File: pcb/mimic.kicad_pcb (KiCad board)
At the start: 6 copper layers, 50.8 x 22.9 mm, 167 parts, among them J1 Conn_01x12_Male, J2 Conn_01x16_Male, J3 USB_B_Micro, J4 MicroSd, J5 JST, J6 JTAG, SW1 SW_Push, U1 FAN53541, U10 NCP115-2.5, U2 FAN53541, U3 LFE5U-25F-8MG285C, U4 MT41K64M16TW-107_J-TR, U5 BQ24232, U6 W25Q128JVP, U7 FAN53541, U8 TPS51206, U9 74HC4067BQ

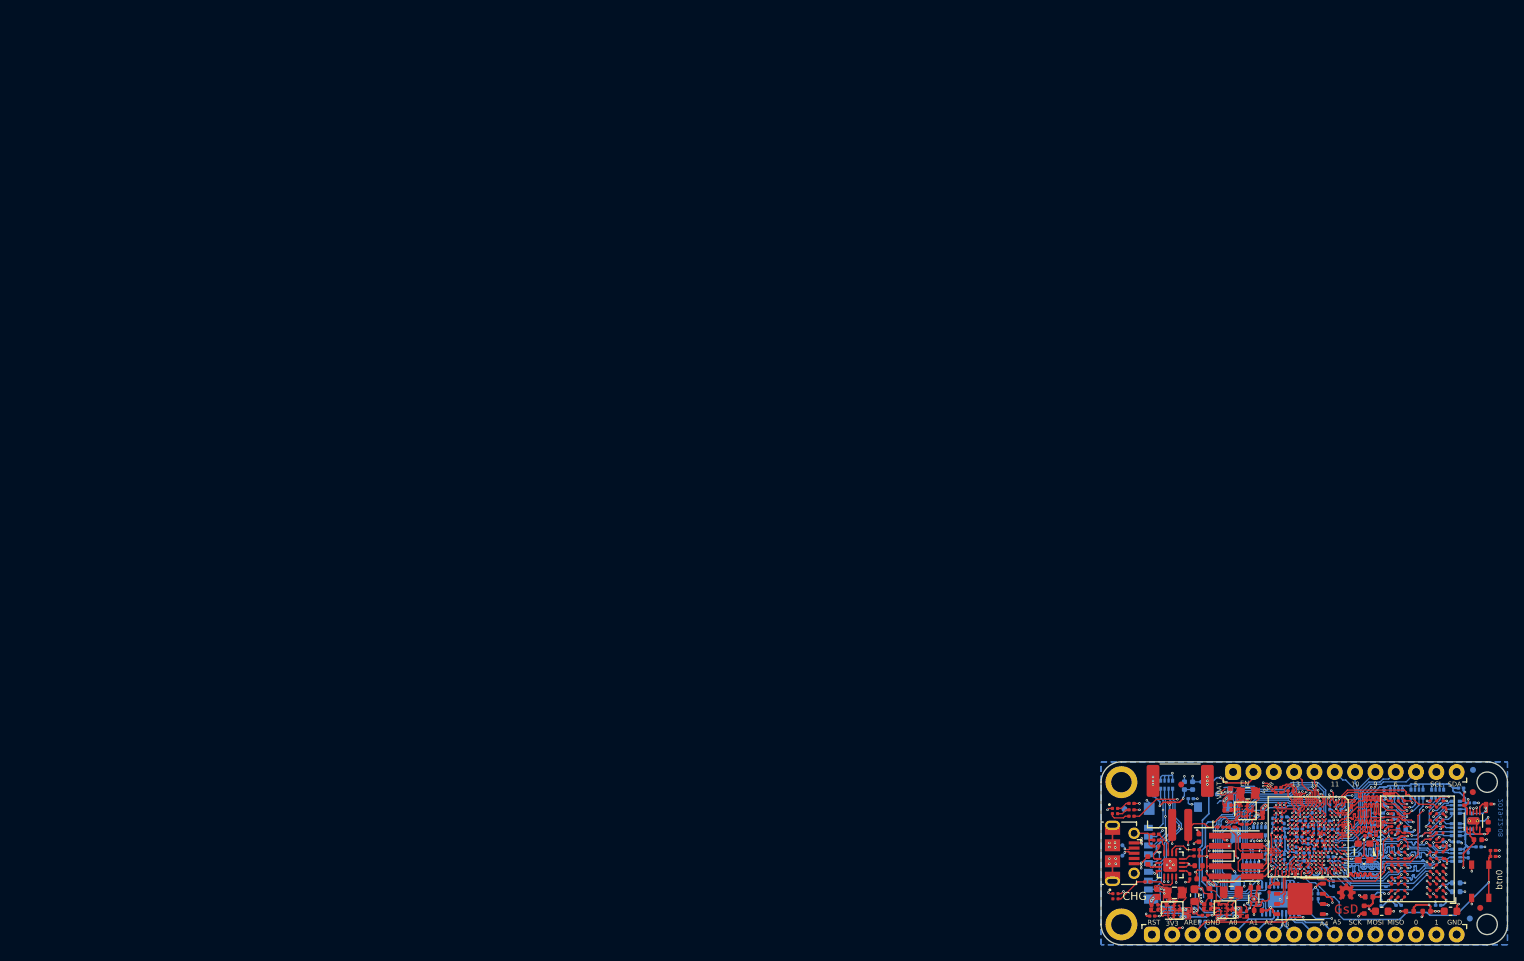
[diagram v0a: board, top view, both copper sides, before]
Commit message: refactor(pcb): strip down
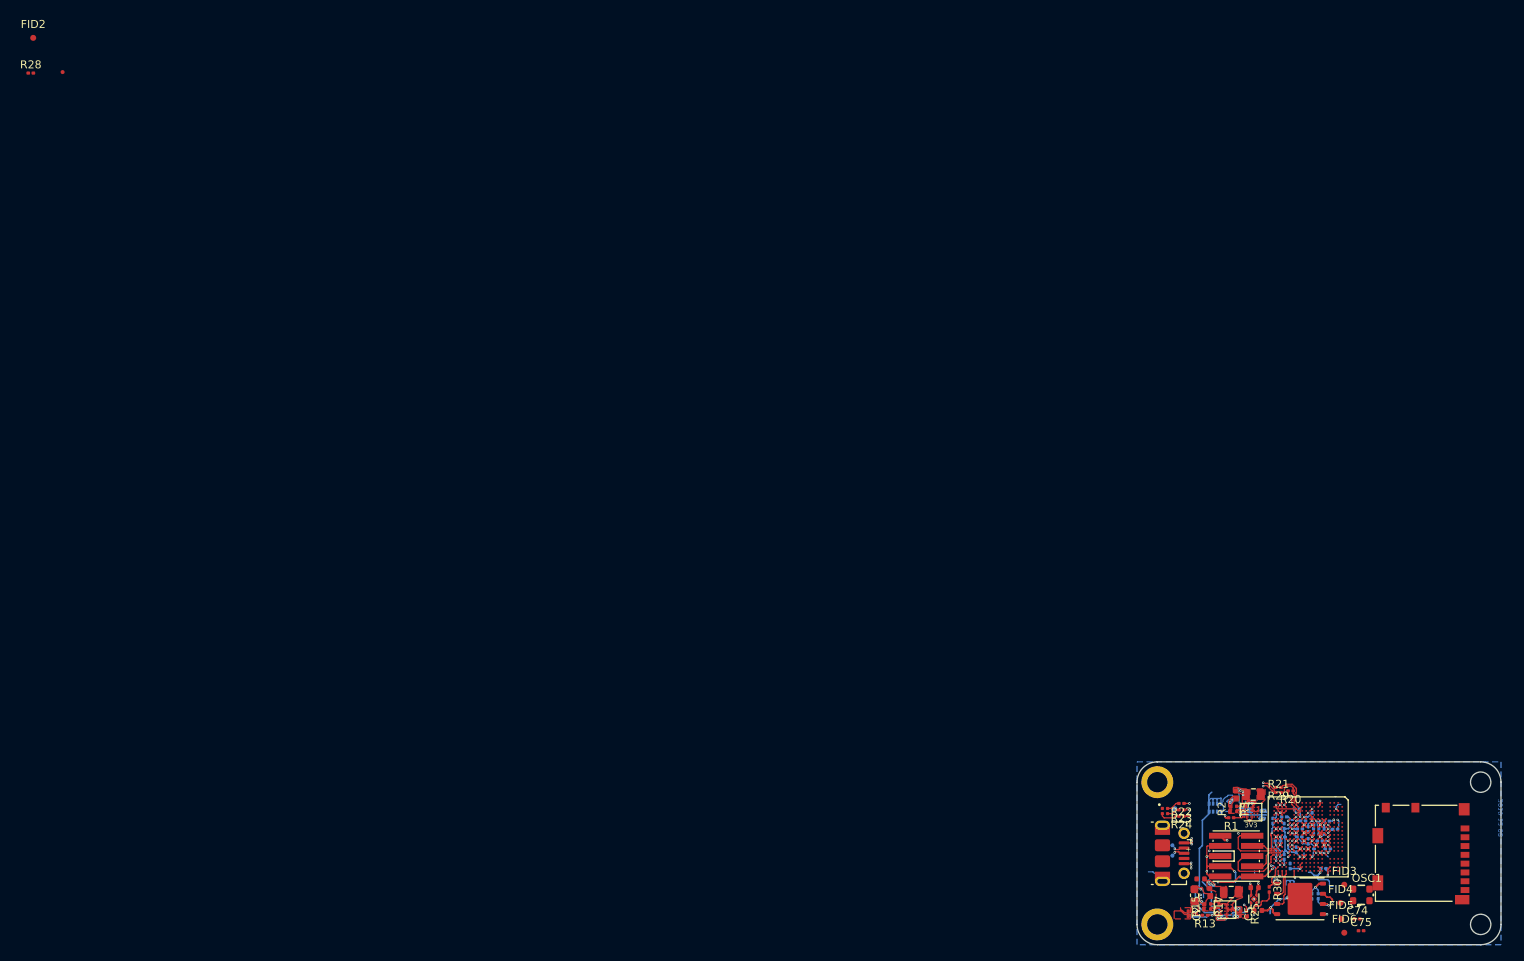
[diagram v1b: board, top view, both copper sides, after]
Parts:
- removed C1, C14, C19, C25, C27, C38, C40, C42, C44, C45, C76: 10nF, gkl_misc:C_0201_0603Metric
- removed C10: 0.22uF, gkl_misc:C_0201_0603Metric
- removed C11, C16, C18, C29, C8: 10uF, Capacitor_SMD:C_0402_1005Metric
- removed C12, C13, C77: 4.7uF, Capacitor_SMD:C_0402_1005Metric
- removed C20, C26, C28, C30, C31, C32, C33, C39, C4, C41, C43, C70, C71, C9: 100nF, gkl_misc:C_0201_0603Metric
- removed C21, C22, C34, C35, C36, C37: 1uF, Capacitor_SMD:C_0402_1005Metric
- removed C23, C24: 22uF, Capacitor_SMD:C_0603_1608Metric
- removed D2: LED_ARGB, gkl_led:0404LED_RGB
- removed FB1, FB2, FB3: 600R, Inductor_SMD:L_0402_1005Metric
- removed G***: LOGO, gkl_logos:oshw_small
- removed G***: LOGO, LOGO
- removed G***: LOGO, logo
- removed J1: Conn_01x12_Male, gkl_conn:Feather_PinHeader_1x12
- removed J2: Conn_01x16_Male, gkl_conn:Feather_PinHeader_1x16
- removed J5: JST, gkl_conn:JST_PH_B2B-PH-SM4-TB_1x02-1MP_P2.00mm_Vertical
- removed L3: 0.47uH, Inductor_SMD:L_0805_2012Metric
- removed R10: 56.2k, gkl_misc:R_0201_0603Metric
- removed R11: 3.06k, gkl_misc:R_0201_0603Metric
- removed R12: 4.32k, gkl_misc:R_0201_0603Metric
- removed R14, R18: 100k, gkl_misc:R_0201_0603Metric
- removed R16: 147k, gkl_misc:R_0201_0603Metric
- removed R19: 240R, Resistor_SMD:R_0402_1005Metric
- removed R26, R32, R33, R7: 10k, gkl_misc:R_0201_0603Metric
- removed R3, R6: 50R, gkl_misc:R_0201_0603Metric
- removed R4, R8: 4.7k, gkl_misc:R_0201_0603Metric
- removed R9: 3.57k, gkl_misc:R_0201_0603Metric
- removed RN1, RN10, RN2, RN3, RN4, RN5, RN6, RN8: 50R, Resistor_SMD:R_Array_Convex_4x0402
- removed RN9: 10K, Resistor_SMD:R_Array_Convex_4x0402
- removed SW1: SW_Push, gkl_misc:PTS_810_SMT_Switch
- removed TP19, TP20, TP28, TP31, TP33: SMD_TP, gkl_misc:TestPoint_Pad_D0.5mm
- removed U4: MT41K64M16TW-107_J-TR, Package_BGA:BGA-96_9.0x13.0mm_Layout2x3x16_P0.8mm
- removed U5: BQ24232, Package_DFN_QFN:QFN-16-1EP_3x3mm_P0.5mm_EP1.75x1.75mm
- removed U7: FAN53541, Package_CSP:WLCSP-20_1.934x2.434mm_Layout4x5_P0.4mm
- removed U8: TPS51206, gkl_housings_dfn:WSON-10-1EP_2x2mm_P0.4mm
- removed U9: 74HC4067BQ, Package_DFN_QFN:Texas_RGY_R-PVQFN-N24_EP2.05x3.1mm
- C2, C48, C49, C5, C50, C51, C52, C53, C54, C55, C56, C57, C58, C59, C60, C61, C62, C63, C64, C65, C66, C67, C68, C69, C74, C75: footprint gkl_misc:C_0201_0603Metric -> Capacitor_SMD:C_0201_0603Metric
- FID3, FID5, J4, TP29: moved to F.Cu
- R1, R13, R15, R17, R2, R20, R21, R22, R23, R24, R25, R27, R29, R30, R31, R5: footprint gkl_misc:R_0201_0603Metric -> Resistor_SMD:R_0201_0603Metric
- R28: footprint gkl_misc:R_0201_0603Metric -> Resistor_SMD:R_0201_0603Metric; moved to F.Cu
- U3: footprint bosonFrameGrabber:csBGA_132 -> gkl_housings_bga:csBGA285
- moved FID2 171.2 mm to (1.02, 1.02)
- moved R28 171.0 mm to (0.72, 5.42), turned to 0 degrees
- moved TP29 167.7 mm to (4.70, 5.30)
- moved J4 39.6 mm to (180.0, 103.0)
- moved FID6 23.8 mm to (164.9, 112.9)
- moved FID3 21.6 mm to (164.9, 106.9)
- moved FID4 17.5 mm to (164.4, 109.2)
- moved FID5 16.1 mm to (164.5, 111.2)
- moved C6 15.8 mm to (151.4, 95.6)
- moved C7 15.8 mm to (152.6, 97.5)
- moved L2 15.8 mm to (153.6, 95.6)
- moved R1 15.8 mm to (150.8, 98.5)
- moved R5 15.8 mm to (151.5, 97.4)
- moved R2 15.8 mm to (150.7, 97.4)
- moved U2 15.8 mm to (153.3, 97.8)
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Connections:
- C62 pad 1: P1.35V -> P3.3V
- C64 pad 1: P1.35V -> P3.3V
- C66 pad 1: P1.35V -> P3.3V
- C68 pad 1: P1.35V -> P3.3V
- J3 pad 4: Net-(J3-Pad4) -> unconnected-(J3-ID-Pad4)
- J4 pad 4: Net-(C29-Pad2) -> unconnected-(J4-Pin_4-Pad4)
- U3 pad A10: SPI_0 -> unconnected-(U3A-PT27B/PCLKC0_1-PadA10)
- U3 pad A11: SPI_2 -> unconnected-(U3A-PT27A/PCLKT0_1-PadA11)
- U3 pad A12: RAM_CS# -> unconnected-(U3F-PL5A-PadA12)
- U3 pad A13: RAM_D7 -> unconnected-(U3F-PL14B-PadA13)
- U3 pad A15: RAM_D4 -> unconnected-(U3F-PL14D-PadA15)
- U3 pad A16: RAM_UDQS- -> unconnected-(U3F-PL20B-PadA16)
- U3 pad A17: RAM_D6 -> unconnected-(U3F-PL23A/PCLKT7_1-PadA17)
- U3 pad A2: RAM_A14 -> unconnected-(U3C-PR20C/GR_PCLK2_0-PadA2)
- U3 pad A3: RAM_A3 -> unconnected-(U3C-PR20A/GR_PCLK2_1-PadA3)
- U3 pad A4: RAM_A4 -> unconnected-(U3C-PR11B-PadA4)
- U3 pad A6: RAM_BA2 -> unconnected-(U3C-PR11A-PadA6)
- U3 pad A7: RAM_A10 -> unconnected-(U3C-PR8B-PadA7)
- U3 pad A8: IO_11 -> unconnected-(U3B-PT35B/PCLKC1_0-PadA8)
- U3 pad B1: RAM_A8 -> unconnected-(U3C-PR23B/PCLKC2_1-PadB1)
- U3 pad B10: IO_5 -> unconnected-(U3A-PT29A/PCLKT0_0-PadB10)
- U3 pad B11: SPI_3 -> unconnected-(U3A-PT4A-PadB11)
- U3 pad B12: RAM_WE# -> unconnected-(U3F-PL2B-PadB12)
- U3 pad B13: RAM_D5 -> unconnected-(U3F-PL14A-PadB13)
- U3 pad B15: RAM_UDQS+ -> unconnected-(U3F-PL20A/GR_PCLK7_1-PadB15)
- U3 pad B17: RAM_D2 -> unconnected-(U3F-PL23B/PCLKC7_1-PadB17)
- U3 pad B18: P1.35V -> unconnected-(U3F-PL23C/PCLKT7_0-PadB18)
- U3 pad B2: RAM_A7 -> unconnected-(U3C-PR20B-PadB2)
- U3 pad B4: ECP5_VREF -> unconnected-(U3C-PR14C/VREF1_2-PadB4)
- U3 pad B6: RAM_A12 -> unconnected-(U3C-PR8A-PadB6)
- U3 pad B7: RAM_BA1 -> unconnected-(U3C-PR2B/S0_IN-PadB7)
- U3 pad B8: IO_10 -> unconnected-(U3B-PT67A-PadB8)
- U3 pad B9: IO_6 -> unconnected-(U3B-PT33A/PCLKT1_1-PadB9)
- U3 pad C1: RAM_A13 -> unconnected-(U3C-PR23C/PCLKT2_0-PadC1)
- U3 pad C10: IO_SDA -> unconnected-(U3A-PT29B/PCLKC0_0-PadC10)
- U3 pad C11: SPI_1 -> unconnected-(U3A-PT4B-PadC11)
- U3 pad C12: RAM_RAS# -> unconnected-(U3F-PL2A-PadC12)
- U3 pad C13: RAM_ODT -> unconnected-(U3F-PL8B-PadC13)
- U3 pad C15: ECP5_VREF -> unconnected-(U3F-PL14C/VREF1_7-PadC15)
- U3 pad C16: RAM_D3 -> unconnected-(U3F-PL20C/GR_PCLK7_0-PadC16)
- U3 pad C17: RAM_D0 -> unconnected-(U3F-PL23D/PCLKC7_0-PadC17)
- U3 pad C18: RAM_D13 -> unconnected-(U3E-PL26B/PCLKC6_1-PadC18)
- U3 pad C2: RAM_A11 -> unconnected-(U3C-PR17B-PadC2)
- U3 pad C3: RAM_A6 -> unconnected-(U3C-PR14D-PadC3)
- U3 pad C4: RAM_A0 -> unconnected-(U3C-PR14B-PadC4)
- U3 pad C6: P1.35V -> unconnected-(U3C-PR5B-PadC6)
- U3 pad C7: RAM_A15 -> unconnected-(U3C-PR2A-PadC7)
- U3 pad C8: IO_9 -> unconnected-(U3B-PT67B-PadC8)
- U3 pad C9: IO_SCL -> unconnected-(U3B-PT33B/PCLKC1_1-PadC9)
- U3 pad D1: RAM_A9 -> unconnected-(U3C-PR23D/PCLKC2_0-PadD1)
- U3 pad D13: RAM_CAS# -> unconnected-(U3F-PL8A-PadD13)
- U3 pad D15: RAM_D1 -> unconnected-(U3F-PL17A-PadD15)
- U3 pad D16: RAM_UDM -> unconnected-(U3F-PL17B-PadD16)
- U3 pad D17: P1.35V -> unconnected-(U3E-PL26A/PCLKT6_1-PadD17)
- U3 pad D18: RAM_CKE -> unconnected-(U3E-PL26C/PCLKT6_0-PadD18)
- U3 pad D2: RAM_A1 -> unconnected-(U3C-PR23A/PCLKT2_1-PadD2)
- U3 pad D3: RAM_A2 -> unconnected-(U3C-PR17A-PadD3)
- U3 pad D4: RAM_A5 -> unconnected-(U3C-PR14A-PadD4)
- U3 pad D6: RAM_BA0 -> unconnected-(U3C-PR5A-PadD6)
- U3 pad F1: ADC_CTRL1 -> unconnected-(U3D-PR35C-PadF1)
- U3 pad F15: RAM_D11 -> unconnected-(U3E-PL29C/GR_PCLK6_1-PadF15)
- U3 pad F16: RAM_D9 -> unconnected-(U3E-PL29B-PadF16)
- U3 pad F17: RAM_D8 -> unconnected-(U3E-PL29A/GR_PCLK6_0-PadF17)
- U3 pad F18: RAM_D15 -> unconnected-(U3E-PL26D/PCLKC6_0-PadF18)
- U3 pad F2: ADC_MUX2 -> unconnected-(U3D-PR32A-PadF2)
- U3 pad F3: ADC_MUX1 -> unconnected-(U3D-PR26D/PCLKC3_0-PadF3)
- U3 pad F4: ADC_MUX0 -> unconnected-(U3D-PR26C/PCLKT3_0-PadF4)
- U3 pad G1: ADC_CTRL0 -> unconnected-(U3D-PR32B-PadG1)
- U3 pad G14: P1.35V -> P3.3V
- U3 pad G15: RAM_D10 -> unconnected-(U3E-PL35A-PadG15)
- U3 pad G16: RAM_LDM -> unconnected-(U3E-PL29D-PadG16)
- U3 pad G18: RAM_LDQS+ -> unconnected-(U3E-PL32A-PadG18)
- U3 pad G3: ADC_SENSE_LO -> unconnected-(U3D-PR29B-PadG3)
- U3 pad G4: IO_A4 -> unconnected-(U3D-PR26B/PCLKC3_1-PadG4)
- U3 pad G5: P1.35V -> P3.3V
- U3 pad H1: ADC_MUX3 -> unconnected-(U3D-PR35D-PadH1)
- U3 pad H14: P1.35V -> P3.3V
- U3 pad H15: ECP5_VREF -> unconnected-(U3E-PL35B/VREF1_6-PadH15)
- U3 pad H16: RAM_D14 -> unconnected-(U3E-PL35C-PadH16)
- U3 pad H17: RAM_LDQS- -> unconnected-(U3E-PL32B-PadH17)
- U3 pad H18: Net-(U3-PadH18) -> unconnected-(U3E-PL38D-PadH18)
- U3 pad H2: IO_12 -> unconnected-(U3D-PR29D-PadH2)
- U3 pad H3: ADC_SENSE_HI -> unconnected-(U3D-PR29A/GR_PCLK3_0-PadH3)
- U3 pad H4: IO_A3 -> unconnected-(U3D-PR26A/PCLKT3_1-PadH4)
- U3 pad H5: P1.35V -> P3.3V
- U3 pad J16: RAM_D12 -> unconnected-(U3E-PL35D-PadJ16)
- U3 pad J17: USER_BUTTON -> unconnected-(U3E-PL38C-PadJ17)
- U3 pad J18: RAM_CK+ -> unconnected-(U3E-PL41A-PadJ18)
- U3 pad J2: IO_13 -> unconnected-(U3D-PR35A-PadJ2)
- U3 pad K15: P1.35V -> unconnected-(U3E-PL41D-PadK15)
- U3 pad K16: P1.35V -> unconnected-(U3E-PL41C-PadK16)
- U3 pad K17: P1.35V -> unconnected-(U3E-PL44A-PadK17)
- U3 pad K18: RAM_CK- -> unconnected-(U3E-PL41B-PadK18)
- U3 pad L18: RAM_RESET# -> unconnected-(U3E-PL44B-PadL18)
- U3 pad L4: IO_A0 -> unconnected-(U3D-PR38B-PadL4)
- U3 pad M14: P1.35V -> P3.3V
- U3 pad M16: EXT_PLL+ -> unconnected-(U3E-PL47C/LLC_GPLL0T_IN-PadM16)
- U3 pad M17: EXT_PLL- -> unconnected-(U3E-PL47D/LLC_GPLL0C_IN-PadM17)
- U3 pad M18: IO_1 -> unconnected-(U3G-PB6B/D4/MOSI2/IO4-PadM18)
- U3 pad N14: P1.35V -> P3.3V
- U3 pad N15: IO_MISO -> unconnected-(U3G-PB4A/D7/IO7-PadN15)
- U3 pad N16: IO_MOSI -> unconnected-(U3G-PB4B/D6/IO6-PadN16)
- U3 pad N17: IO_0 -> unconnected-(U3G-PB6A/D5/MISO2/IO5-PadN17)
- U3 pad N3: IO_A1 -> unconnected-(U3D-PR38D-PadN3)
- U3 pad N4: IO_A2 -> unconnected-(U3D-PR38C-PadN4)
- U3 pad R16: Net-(U3-PadR16) -> unconnected-(U3G-PB18A/WRITEN-PadR16)
- U3 pad R17: IO_SCK -> unconnected-(U3G-PB13A/SN/CSN-PadR17)
- U3 pad T17: IO_A5 -> unconnected-(U3G-PB13B/CS1N-PadT17)
- U3 pad U15: Net-(U3-PadU15) -> unconnected-(U3H-DONE-PadU15)
- U3 pad V11: Net-(U3-PadV11) -> unconnected-(U3H-RESERVED-PadV11)
- U3 pad V12: Net-(U3-PadV12) -> unconnected-(U3H-RESERVED-PadV12)
- U3 pad V16: Net-(U3-PadV16) -> unconnected-(U3H-INITN-PadV16)
- U3 pad V2: Net-(U3-PadV2) -> unconnected-(U3H-RESERVED-PadV2)
- U3 pad V3: Net-(U3-PadV3) -> unconnected-(U3H-RESERVED-PadV3)
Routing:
- net GND: track 236.6 -> 131.9 mm, vias 153 -> 76
- net P1.35V: track 97.8 -> 0.00 mm, vias 18 -> 0
- net ECP5_VREF: track 59.4 -> 0.00 mm, vias 9 -> 0
- net VTT: track 53.8 -> 0.00 mm, vias 1 -> 0
- net /sheetPower/PGOOD_P1.35V: track 44.4 -> 0.00 mm, vias 3 -> 0
- net ADC_MUX1: track 39.4 -> 0.00 mm, vias 1 -> 0
- net ADC_MUX0: track 38.2 -> 0.00 mm, vias 1 -> 0
- net USER_BUTTON: track 36.4 -> 0.00 mm, vias 2 -> 0
- net SD0_DAT0: track 33.8 -> 0.00 mm, vias 2 -> 0
- net SD0_DAT1: track 33.3 -> 0.00 mm, vias 2 -> 0
- net /sheetIO/A5: track 32.8 -> 0.00 mm, vias 1 -> 0
- net VSYS: track 48.7 -> 15.9 mm, vias 13 -> 7
- net ADC_CTRL1: track 32.0 -> 0.00 mm, vias 1 -> 0
- net ADC_MUX3: track 31.2 -> 0.00 mm, vias 1 -> 0
- net ADC_MUX2: track 29.8 -> 0.00 mm, vias 1 -> 0
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- removed copper zone on In3.Cu, net /sheetHyperRAM/RAM_VDD
- removed copper zone on In3.Cu, net /sheetHyperRAM/RAM_VDDQ
- removed copper zone on F.Cu, net ECP5_VREF
- removed copper zone on In3.Cu, net ECP5_VREF
- removed copper zone on F.Cu, net Net-(L3-Pad1)
- removed copper zone on F.Cu, net Net-(R16-Pad1)
- removed copper zone on B.Cu, net P1.35V
- removed copper zone on F.Cu, net P1.35V
- removed copper zone on In1.Cu, net P1.35V
- removed copper zone on In2.Cu, net P1.35V
- removed copper zone on In3.Cu, net P1.35V
- removed copper zone on In4.Cu, net P1.35V
- removed copper zone on In3.Cu, net VBATT
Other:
- board size 50.8 x 22.9 mm -> 45.5 x 22.9 mm
- board text removed: "0"
- board text removed: "1"
- board text removed: "10"
- board text removed: "11"
- board text removed: "12"
- board text removed: "13"
- board text removed: "5"
- board text removed: "6"
- board text removed: "9"
- board text removed: "A0"
- board text removed: "A1"
- board text removed: "A2"
- board text removed: "A3"
- board text removed: "A4"
- board text removed: "A5"
- board text removed: "AREF"
- board text removed: "CHG"
- board text removed: "EN"
- board text removed: "GND"
- board text removed: "MISO"
- board text removed: "MOSI"
- board text removed: "RST"
- board text removed: "SCK"
- board text removed: "SCL"
- board text removed: "SDA"
- board text removed: "VBAT"
- board text removed: "VUSB"
- board text removed: "btn0"
- board text removed: "r0.2"
